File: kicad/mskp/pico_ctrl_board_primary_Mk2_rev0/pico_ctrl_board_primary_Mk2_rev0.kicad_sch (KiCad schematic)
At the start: 24 parts, among them J1 USB_C_I2C_Receptacle, J2 SPI-JST, J3 RJ45_I2C_SPI_Port, J4 UART-JST, J5 I2C-aux-pad, J6 OLED_128x64, J7 Keypad-Matrix_JST, J8 USB-sw-ctrl, J9 Debug_pads, SW1 RESET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

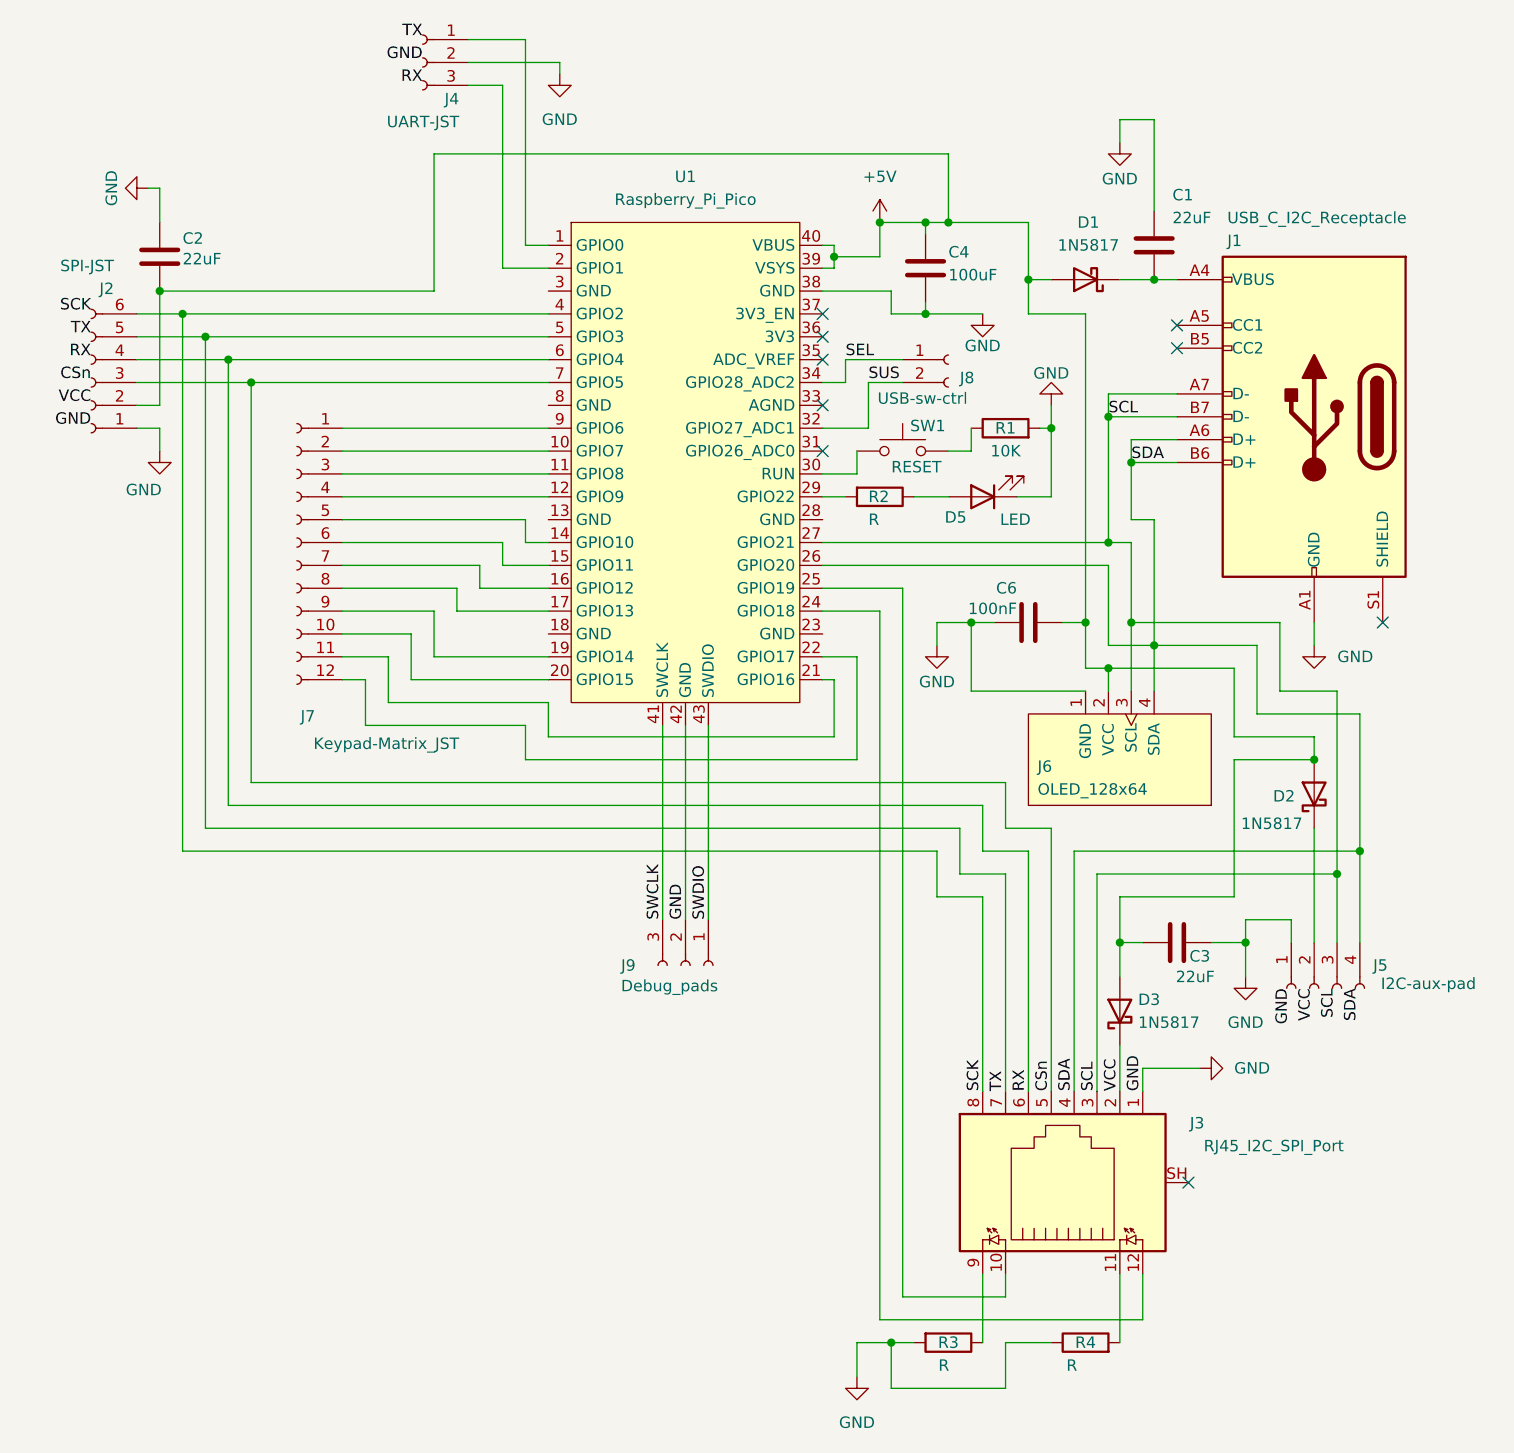
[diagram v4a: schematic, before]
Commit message: Refining PCB outlines for pico and io control boards
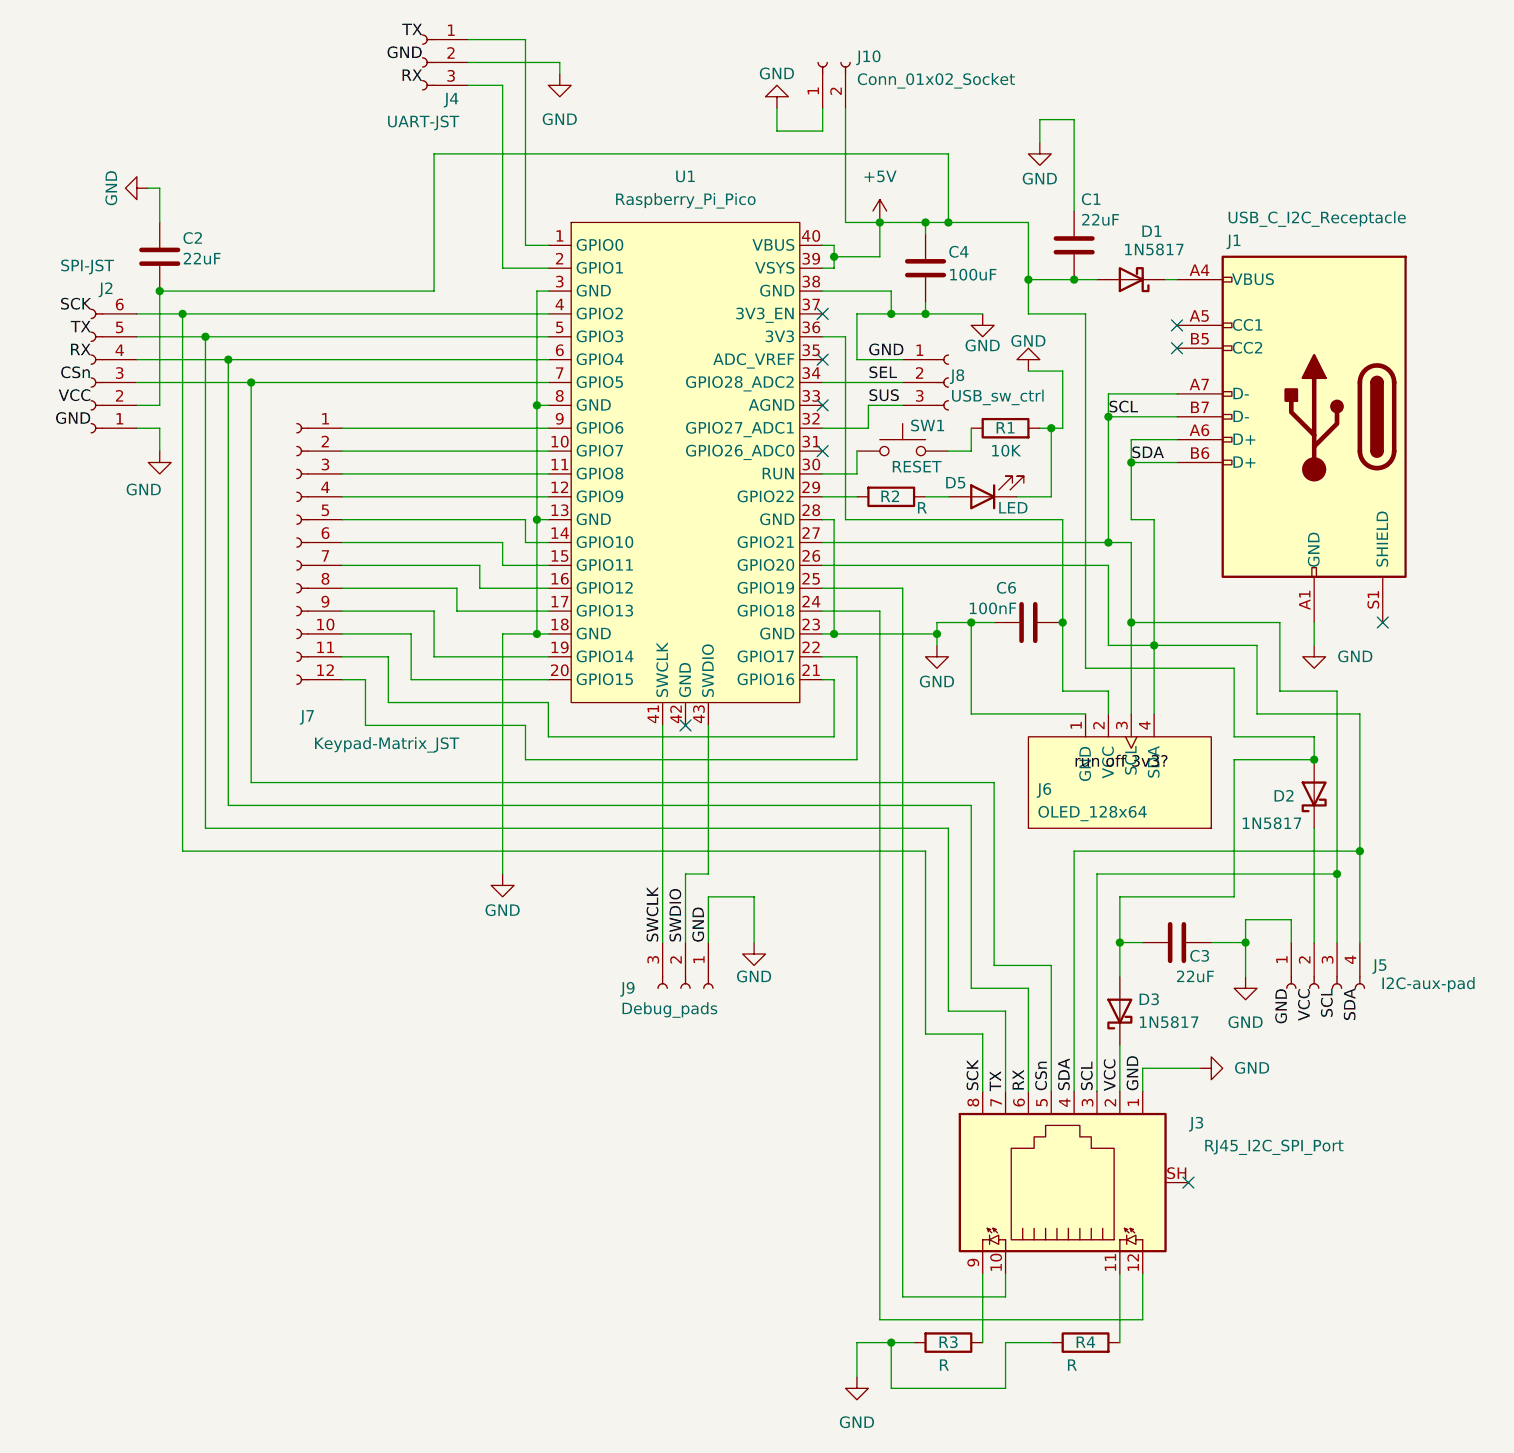
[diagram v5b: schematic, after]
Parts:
- removed J8: USB-sw-ctrl, Connector_PinHeader_2.54mm:PinHeader_1x02_P2.54mm_Vertical, symbol Connector:Conn_01x02_Socket
- added J10: Conn_01x02_Socket, Connector_PinHeader_2.54mm:PinHeader_1x02_P2.54mm_Vertical, symbol Connector:Conn_01x02_Socket
- added J8: USB_sw_ctrl, Connector_PinSocket_2.54mm:PinSocket_1x03_P2.54mm_Vertical, symbol Connector:Conn_01x03_Socket
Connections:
- net +5V: now also C1.1, J10.2 (Pin_2); no longer C6.1, J6.2 (VCC)
- net GND: now also J9.1 (Pin_1), U1.13 (GND), U1.18 (GND), U1.23 (GND), U1.28 (GND), U1.3 (GND), U1.8 (GND), J10.1 (Pin_1), J8.1 (Pin_1); no longer J9.2 (Pin_2), U1.42 (GND)
- net SEL: now also J8.2 (Pin_2)
- net SUS: now also J8.3 (Pin_3)
- net SWDIO: now also J9.2 (Pin_2); no longer J9.1 (Pin_1)
- net at D1.1 (K), J1.A4 (VBUS), J1.A9 (VBUS)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: no longer C1.1
- net at U1.36 (3V3): now also C6.1, J6.2 (VCC)
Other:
- moved on the sheet: C1, D1, J6, J9, R2

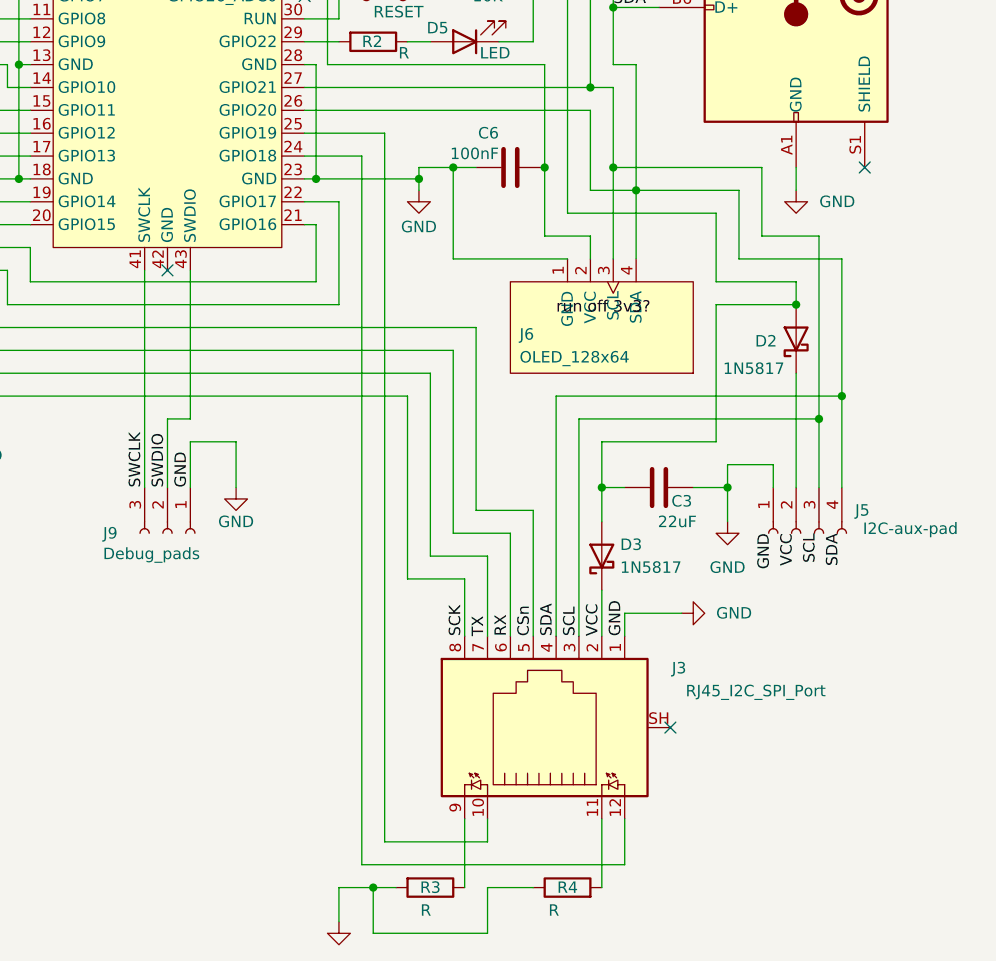
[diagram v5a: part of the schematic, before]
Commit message: Initial layout work on pico_ctrl_board_primary_Mk2_rev0 PCB
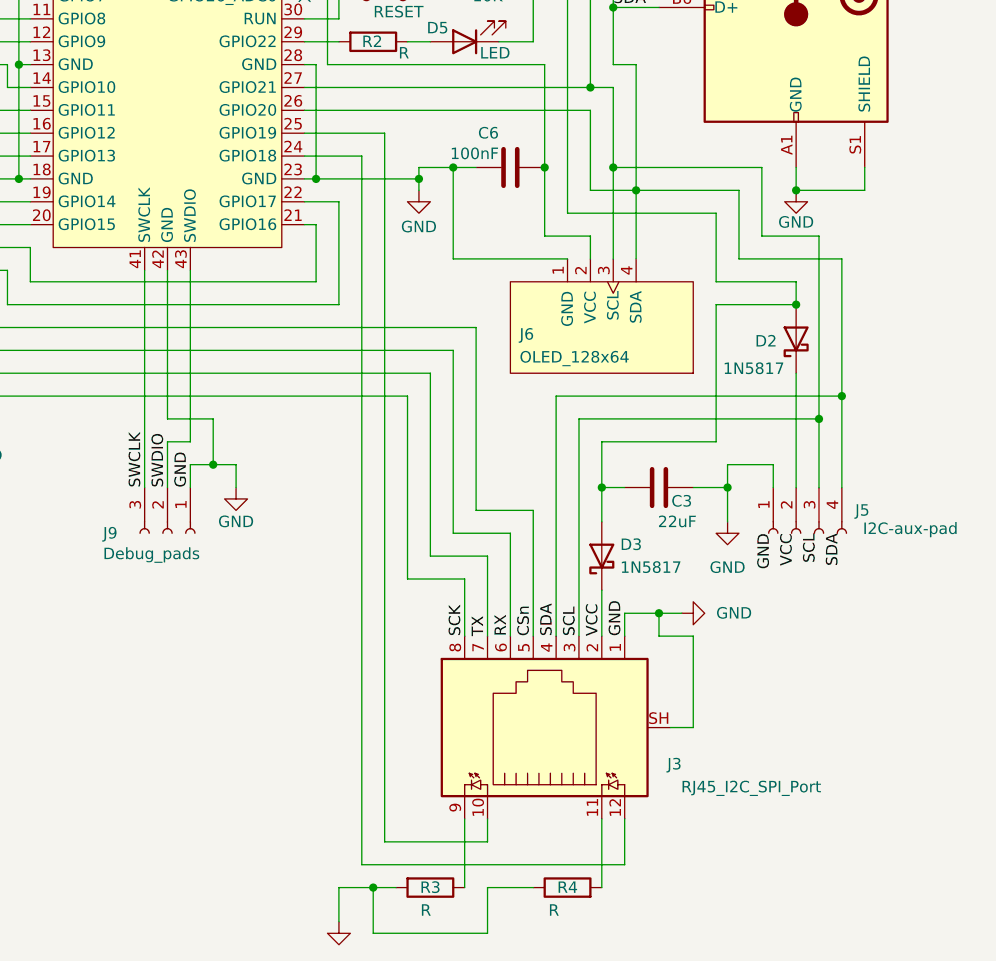
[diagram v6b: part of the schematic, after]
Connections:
- net GND: now also J1.S1 (SHIELD), J3.SH, U1.42 (GND)
- no-connect marks 9 -> 6
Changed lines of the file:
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@@
 	)
 	(junction
+		(at 123.19 120.65)
+		(diameter 0)
+		(color 0 0 0 0)
+	)
+	(junction
 		(at 165.1 64.77)
 		(diameter 0)
@@
 	)
 	(junction
+		(at 187.96 90.17)
+		(diameter 0)
+		(color 0 0 0 0)
+	)
+	(junction
 		(at 144.78 43.18)
 		(diameter 0)
@@
 	)
 	(junction
+		(at 172.72 137.16)
+		(diameter 0)
+		(color 0 0 0 0)
+	)
+	(junction
 		(at 101.6 88.9)
 		(diameter 0)
@@
 	)
 	(no_connect
-		(at 173.99 149.86)
-	)
-	(no_connect
 		(at 133.35 68.58)
 	)
-	(no_connect
-		(at 195.58 87.63)
-	)
-	(no_connect
-		(at 118.11 99.06)
-	)
 	(wire
 		(pts
@@
 	(wire
 		(pts
-			(xy 125.73 118.11) (xy 125.73 123.19)
+			(xy 125.73 120.65) (xy 125.73 123.19)
 		)
 		(stroke
@@
 	(wire
 		(pts
-			(xy 120.65 99.06) (xy 120.65 115.57)
+			(xy 120.65 99.06) (xy 120.65 118.11)
 		)
 		(stroke
@@
 	(wire
 		(pts
+			(xy 173.99 149.86) (xy 176.53 149.86)
+		)
+		(stroke
+			(width 0)
+			(type default)
+		)
+	)
+	(wire
+		(pts
 			(xy 133.35 55.88) (xy 135.89 55.88)
 		)
@@
 	(wire
 		(pts
-			(xy 120.65 115.57) (xy 118.11 115.57)
+			(xy 176.53 139.7) (xy 172.72 139.7)
+		)
+		(stroke
+			(width 0)
+			(type default)
+		)
+	)
+	(wire
+		(pts
+			(xy 120.65 118.11) (xy 118.11 118.11)
 		)
 		(stroke
@@
 	(wire
 		(pts
-			(xy 120.65 118.11) (xy 125.73 118.11)
+			(xy 120.65 120.65) (xy 123.19 120.65)
 		)
 		(stroke
@@
 	(wire
 		(pts
+			(xy 118.11 115.57) (xy 123.19 115.57)
+		)
+		(stroke
+			(width 0)
+			(type default)
+		)
+	)
+	(wire
+		(pts
 			(xy 160.02 66.04) (xy 158.75 66.04)
 		)
@@
 	(wire
 		(pts
+			(xy 123.19 120.65) (xy 125.73 120.65)
+		)
+		(stroke
+			(width 0)
+			(type default)
+		)
+	)
+	(wire
+		(pts
 			(xy 142.24 162.56) (xy 153.67 162.56)
 		)
@@
 	(wire
 		(pts
-			(xy 118.11 115.57) (xy 118.11 123.19)
+			(xy 118.11 118.11) (xy 118.11 123.19)
 		)
 		(stroke
@@
 	(wire
 		(pts
+			(xy 172.72 137.16) (xy 172.72 139.7)
+		)
+		(stroke
+			(width 0)
+			(type default)
+		)
+	)
+	(wire
+		(pts
 			(xy 64.77 110.49) (xy 147.32 110.49)
 		)
@@
 	(wire
 		(pts
-			(xy 120.65 118.11) (xy 120.65 123.19)
+			(xy 120.65 120.65) (xy 120.65 123.19)
 		)
 		(stroke
@@
 	(wire
 		(pts
+			(xy 195.58 87.63) (xy 195.58 90.17)
+		)
+		(stroke
+			(width 0)
+			(type default)
+		)
+	)
+	(wire
+		(pts
 			(xy 139.7 86.36) (xy 139.7 165.1)
 		)
@@
 	(wire
 		(pts
-			(xy 168.91 137.16) (xy 175.26 137.16)
+			(xy 168.91 137.16) (xy 172.72 137.16)
 		)
 		(stroke
@@
 	(wire
 		(pts
+			(xy 118.11 99.06) (xy 118.11 115.57)
+		)
+		(stroke
+			(width 0)
+			(type default)
+		)
+	)
+	(wire
+		(pts
 			(xy 97.79 81.28) (xy 97.79 78.74)
 		)
@@
 	(wire
 		(pts
+			(xy 176.53 149.86) (xy 176.53 139.7)
+		)
+		(stroke
+			(width 0)
+			(type default)
+		)
+	)
+	(wire
+		(pts
 			(xy 158.75 125.73) (xy 158.75 139.7)
 		)
@@
 	(wire
 		(pts
+			(xy 195.58 90.17) (xy 187.96 90.17)
+		)
+		(stroke
+			(width 0)
+			(type default)
+		)
+	)
+	(wire
+		(pts
 			(xy 102.87 96.52) (xy 85.09 96.52)
 		)
@@
 	(wire
 		(pts
+			(xy 123.19 115.57) (xy 123.19 120.65)
+		)
+		(stroke
+			(width 0)
+			(type default)
+		)
+	)
+	(wire
+		(pts
 			(xy 146.05 88.9) (xy 146.05 90.17)
 		)
@@
 	(wire
 		(pts
+			(xy 172.72 137.16) (xy 175.26 137.16)
+		)
+		(stroke
+			(width 0)
+			(type default)
+		)
+	)
+	(wire
+		(pts
 			(xy 100.33 45.72) (xy 100.33 22.86)
 		)
@@
 		)
 	)
-	(label "run off 3v3?"
-		(at 161.29 104.14 0)
-		(fields_autoplaced yes)
-		(effects
-			(font
-				(size 1.27 1.27)
-			)
-			(justify left bottom)
-		)
-	)
 	(label "GND"
 		(at 185.42 128.27 270)
@@
 		)
 		(property "Value" "GND"
-			(at 192.532 91.44 0)
+			(at 187.96 93.726 0)
 			(effects
 				(font
@@
 		(dnp no)
 		(property "Reference" "J3"
-			(at 175.768 143.256 90)
+			(at 175.26 153.924 90)
 			(effects
 				(font
@@
 		)
 		(property "Value" "RJ45_I2C_SPI_Port"
-			(at 191.262 145.796 90)
+			(at 190.754 156.464 90)
 			(effects
 				(font
